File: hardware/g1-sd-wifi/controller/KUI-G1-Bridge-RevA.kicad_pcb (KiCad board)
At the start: 6 copper layers, 59 x 105 mm, 365 parts, among them J10 FPGA JTAG pogo pads, J20 5V/GND direct wire pads, J201 microSD push-pull 1.42mm, J202 RP USB service pads, J203 RP SWD/reset/boot pads, J204 C5 direct UART recovery pads, J40 FH12-14S-0.5SH(55), J41 FH12-6S-0.5SH(55), J50 FH12-20S-0.5SH(55), J51 FH12-20S-0.5SH(55), K201 C5 removable compression cont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, K202 C5 removable compression cont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, K203 C5 removable compression cont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, K204 C5 removable compression cont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, K205 C5 removable compression cont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, K206 C5 removable compression cont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, K207 C5 removable compression cont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, K208 C5 removable compression cont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, K209 C5 removable compression cont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, K210 C5 removable compression cont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, K211 C5 removable compression cont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, K212 C5 removable compression cont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, K213 C5 removable compression cont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, K214 C5 removable compression cont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, K215 C5 removable compression cont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, K216 C5 removable compression cont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, Q20 PMV48XP reverse polarity, Q201 C5 recovery pull-down, Q202 C5 recovery pull-down, U10 LCMXO2-2000HC-4TG100C, U20 TPS2116 automatic mux, U201 RP2350B, U202 16MiB boot NOR, U203 8MiB QSPI PSRAM, U204 C5 off-state isolation, U205 C5 off-state isolation, U207 SD4-bit DAT rail isolation, U208 SD CLK/CMD rail isolation, U209 SD enable/power-good NAND, U21 TPS62162 3.3V 1A, U22 TPS62162 3.3V 1A, U23 TPS3808G33DBVR, U24 TPS3808G33DBVR, U25 TPS3808G33DBVR, U26 TPS3808G01DBVR, U27 SN74LVC2G08DCUR, U28 SN74LVC2G08DCUR, U29 SN74LVC2G08DCUR, U30 SN74LVC1G11DBVR, U31 SN74LVC2G04DBVT, U32 SN74LVC1G32DBVR, U33 SN74LVC1G08DBVR, U34 SN74LVC1G08DBVR, U35 SN74LVC16T245, U36 SN74LVC244A host controls, U37 SN74LVC1G17 host RESETn, U38 SN74LVC1G125 qualified ATA_IN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, U39 SN74LVC1G125 qualified ATA_DM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, U40 MX29LV640ETTI-70G x8 / 4 x 2M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, U41 SN74LVC2G125 bank-domain buff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, U42 SN74LVC1G11 write-authorize A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, U43 SN74LVC1G04 write-block inver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, U44 SN74LVC1G332 NOR WE qualifier, U45 TLV803EB29 console-rail NOR r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, U70 SN74LVC1G07 open-drain IORDY, U71 TPS22919 Wi-Fi input switch, U72 SN74LVC1G32DBVR, U73 SN74LVC1G32DBVR, X10 50MHz 3.3V, X201 12MHz

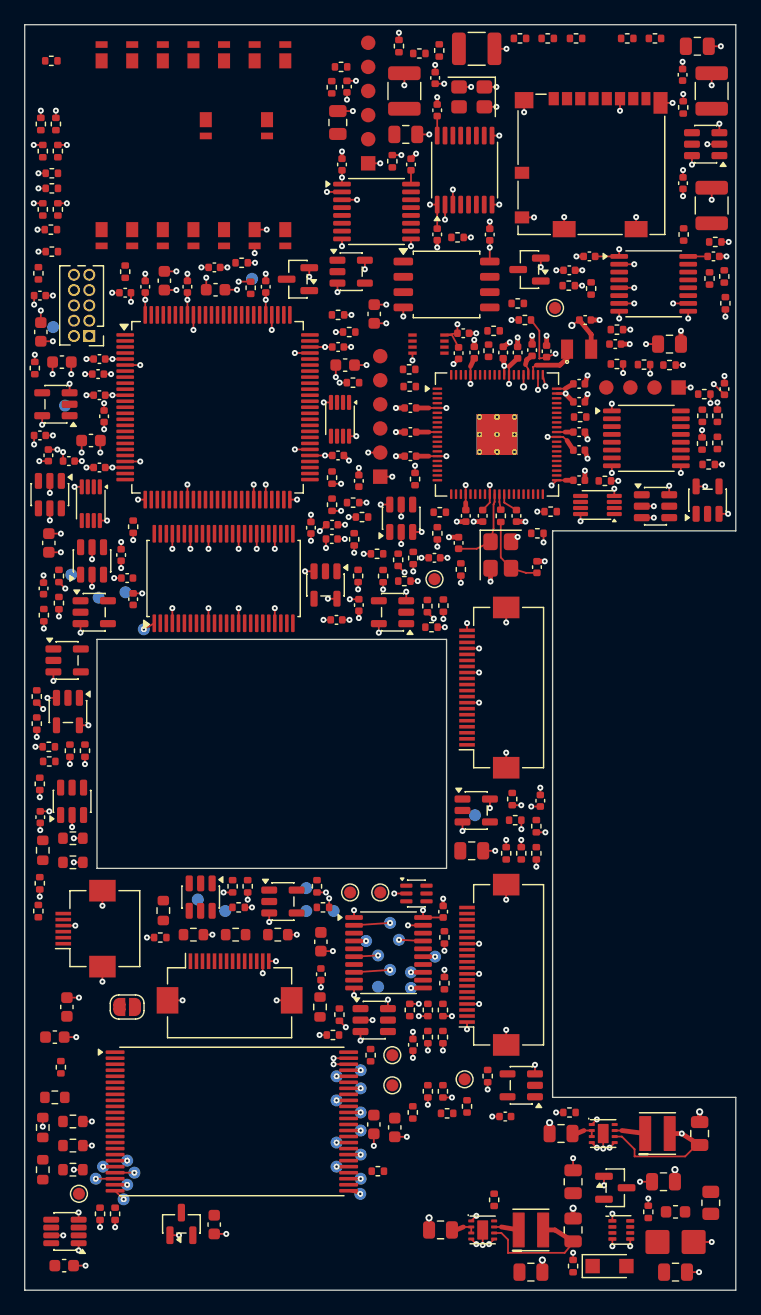
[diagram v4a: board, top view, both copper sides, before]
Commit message: G1 carrier: FPGA pull-downs replace the sixteen BUS_DD biases
The 47 k biases on BUS_DD (between the FPGA and U35's A port) found no
room near that bus and were placed up to 40 mm away; their connections
were a quarter of what the router could not close. The FPGA's own I/O
pull-down now holds BUS_DD during tri-state idle (PULLMODE=DOWN in the
LPF, emitted by sync_fpga_pins.py). Before configuration U35 is held
disabled by its DATA_OEn pull-up; the MachXO2's unconfigured pin state
is to be confirmed against Lattice TN1202 at bring-up. The host-side
ATA_DD biases stay.

- power-bus.json drops R223..R253 (odd); integration counts 349/360/351;
  ERC 0; integration audit passes; parts list BASE 263 fitted parts.
- update_board_from_netlist: --allow-remove deletes a removed part's
  footprint and pad copper.
- floorplan script: removes the biases and places the optional reserve
  bank (C202-C205) beside U20, which it feeds, instead of 90 mm away.
- Board regenerated: 153/153 placed, native DRC 0, parity 0. Routing in
  progress.

Co-Authored-By: Claude Opus 5.5 <noreply@anthropic.com>
Claude-Session: https://claude.ai/code/session_01Gp9EYc2r9fMpZ7V8WtfonZ
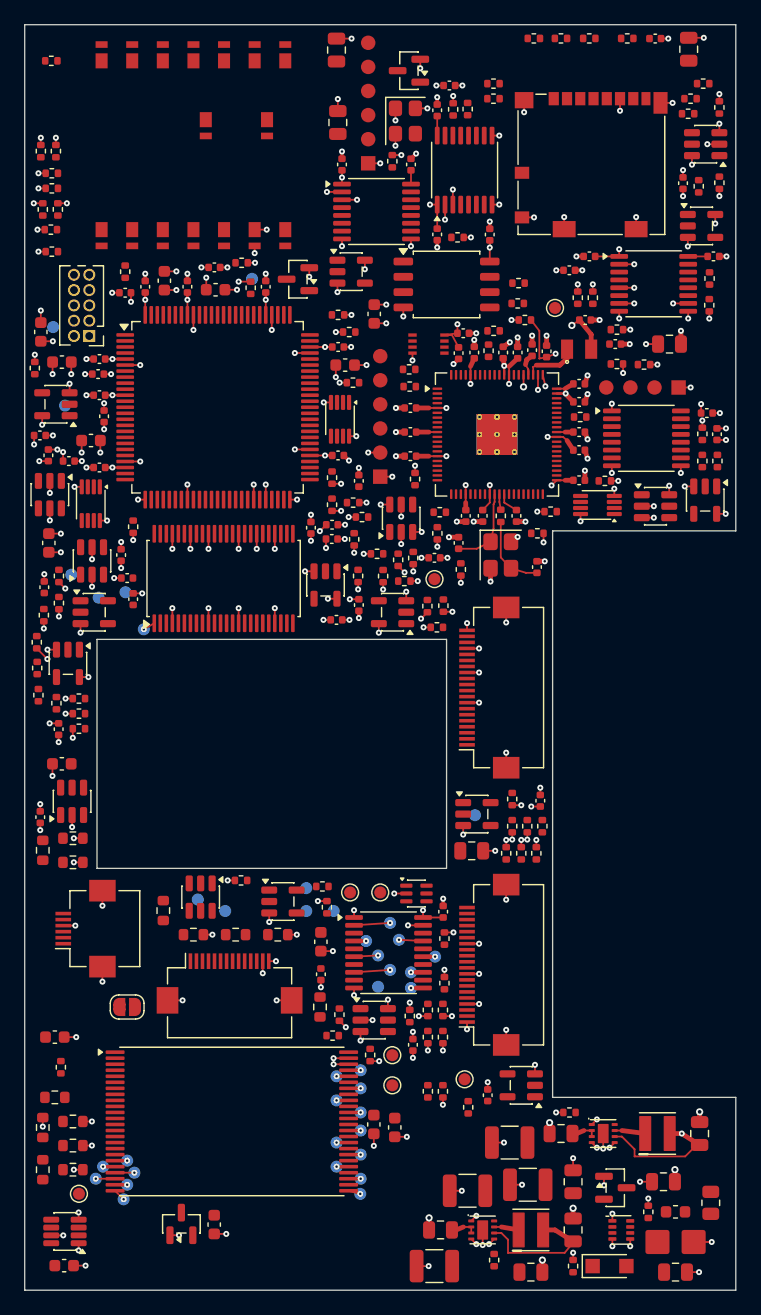
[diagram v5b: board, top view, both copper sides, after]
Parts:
- removed R223, R225, R227, R229, R231, R233, R235, R237, R239, R241, R243, R245, R247, R249, R251, R253: 47k, KUI_Footprints:R_0402_1005Metric
- moved C205 101.1 mm to (104.0, 148.0), turned to 180 degrees
- moved C204 91.4 mm to (106.7, 141.8), turned to 180 degrees
- moved C203 88.8 mm to (110.2, 137.8), turned to 180 degrees
- moved C202 82.7 mm to (111.7, 141.2), turned to 180 degrees
- moved R263 52.7 mm to (88.0, 116.0), turned to 180 degrees
- moved R248 41.6 mm to (74.5, 102.2), turned to 180 degrees
- moved C223 40.3 mm to (126.6, 77.2), turned to 180 degrees
- moved R252 40.3 mm to (74.5, 103.4), turned to 180 degrees
- moved C232 36.0 mm to (72.8, 103.4), turned to -90 degrees
- moved U38 35.9 mm to (107.5, 110.5)
- moved R268 35.0 mm to (71.1, 100.6), turned to 90 degrees
- moved R221 32.8 mm to (71.0, 96.2), turned to 90 degrees
- moved U34 32.0 mm to (126.5, 84.4), turned to -90 degrees
- moved R262 26.1 mm to (113.0, 111.5), turned to -90 degrees
- moved U209 22.8 mm to (126.2, 61.7), turned to 0 degrees
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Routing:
- net GND: track 227.6 -> 217.0 mm, vias 282 -> 266

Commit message: G1 carrier: routed checkpoint, 30 connections open, DRC clean
Freerouting 1.9 (Headless19Ripup, 0.25 mm power escapes, B.Cu priced as
an inner layer) on the re-floorplanned six-layer board, imported natively
with dangling router leftovers removed: 0 DRC violations, schematic
parity 0, 30 connections still open (from 600 on the four-layer board).
Not a release: the open connections, power widening and layout review
remain.

The open 30 are mostly ATA data from U35 to J50/J51, the ATA control
lines from U36 to the FPGA's west edge, and four RP2350 escapes.

- Headless19Ripup: optional net pattern routed first in every pass.
- close_gaps.py: grid A* router for the last open pairs, using KiCad's
  clearance-inflated outlines, no via in SMD lands, native-DRC verified
  (it closes only connections that are blocked by distance, not by
  existing copper; rip-up is left to the autorouter).

Co-Authored-By: Claude Opus 5.5 <noreply@anthropic.com>
Claude-Session: https://claude.ai/code/session_01Gp9EYc2r9fMpZ7V8WtfonZ
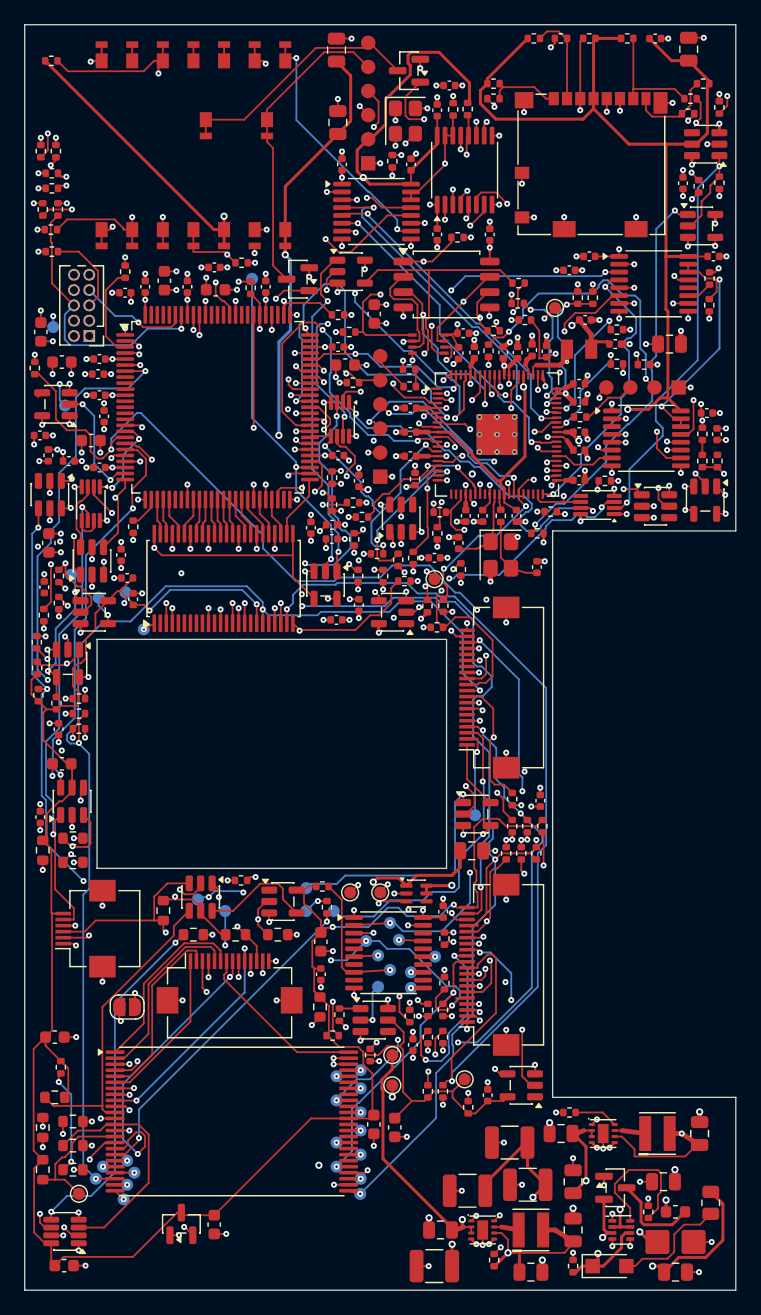
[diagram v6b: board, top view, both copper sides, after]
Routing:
- net CONSOLE_3V3: track 0.00 -> 274.4 mm, vias 0 -> 7
- net +3V3_STORAGE: track 12.8 -> 187.8 mm, vias 0 -> 4
- net ATA_DD15: track 1.00 -> 110.0 mm, vias 1 -> 3
- net BIOS_BANK1: track 0.00 -> 107.1 mm, vias 0 -> 5
- net ATA_DD10: track 1.00 -> 102.2 mm, vias 1 -> 4
- net ATA_DD14: track 1.00 -> 97.1 mm, vias 1 -> 7
- net PWR_FAILn: track 0.00 -> 94.8 mm, vias 0 -> 6
- net ATA_DD12: track 1.60 -> 95.1 mm, vias 1 -> 4
- net ATA_DD9: track 1.00 -> 90.7 mm, vias 1 -> 4
- net +5V_C5: track 0.00 -> 87.4 mm, vias 0 -> 3
- net IORDY_RELEASE: track 0.00 -> 85.7 mm, vias 0 -> 6
- net PRIMARY_5V: track 0.00 -> 84.4 mm, vias 0 -> 4
- net BIOS_BANK0: track 0.00 -> 83.8 mm, vias 0 -> 4
- net BUS_SAFE: track 0.00 -> 80.9 mm, vias 0 -> 5
- net INTRQ_OEn: track 0.00 -> 80.7 mm, vias 0 -> 2
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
